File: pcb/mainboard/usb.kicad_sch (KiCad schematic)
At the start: 22 parts, among them J601 USB_AB_Micro, J602 USB_B_Micro, J604 USB_B_Micro, U100 MCIMX6Y7DVM09AB, U601 USBLC6-2P6, U602 AP2151, U604 CH340N, U605 USBLC6-2P6

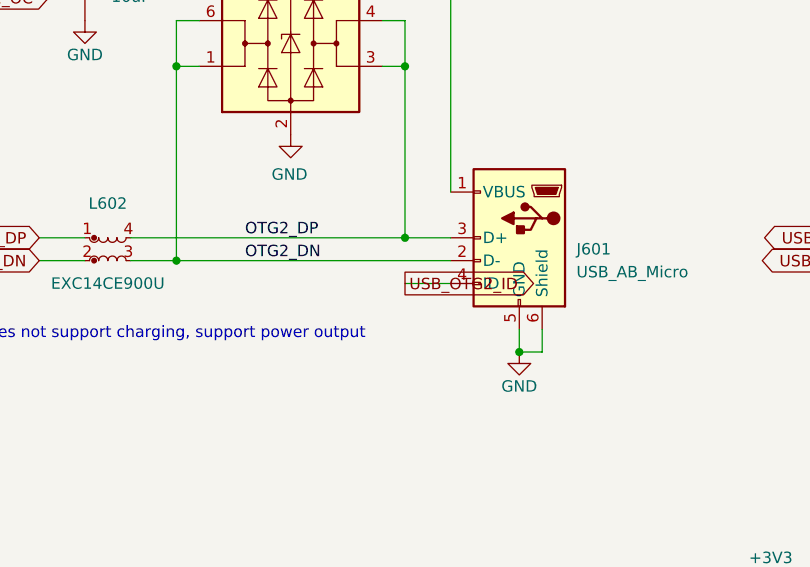
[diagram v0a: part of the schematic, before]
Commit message: pcb: switch to max17135, length tuning for QSPI and SD
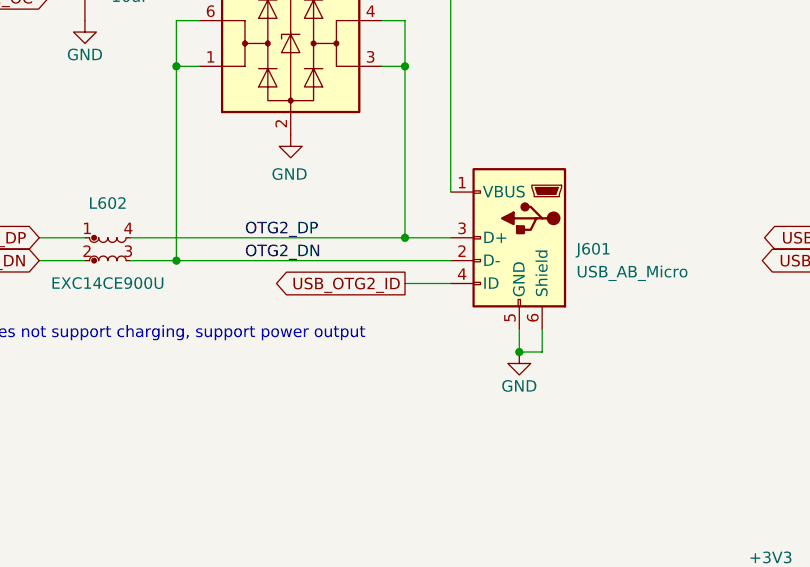
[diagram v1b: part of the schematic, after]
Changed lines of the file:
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@@
     )
   )
-  (global_label "USB_OTG2_ID" (shape output) (at 134.62 78.74 0) (fields_autoplaced)
-    (effects (font (size 1.27 1.27)) (justify left))
-    (property "Intersheet References" "${INTERSHEET_REFS}" (id 0) (at 149.4307 78.6606 0)
-      (effects (font (size 1.27 1.27)) (justify left) hide)
+  (global_label "USB_OTG2_ID" (shape output) (at 134.62 78.74 180) (fields_autoplaced)
+    (effects (font (size 1.27 1.27)) (justify right))
+    (property "Intersheet References" "${INTERSHEET_REFS}" (id 0) (at 119.8093 78.8194 0)
+      (effects (font (size 1.27 1.27)) (justify right) hide)
     )
   )
